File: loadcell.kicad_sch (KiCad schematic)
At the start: 11 parts

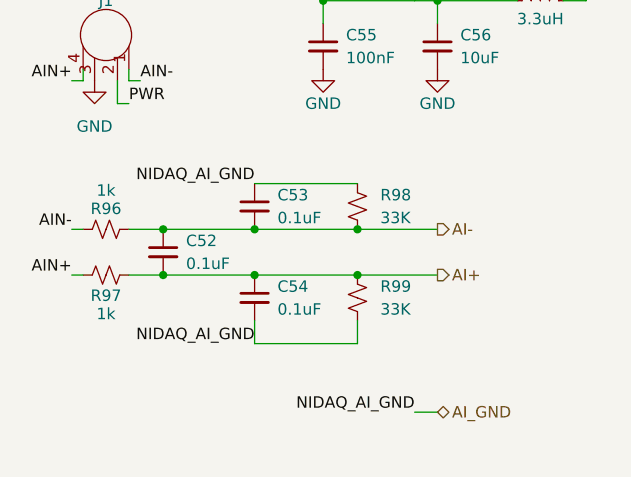
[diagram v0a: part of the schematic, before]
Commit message: Updated schematic. No filtering but besides that finished. Need to fix footprints and start layout.
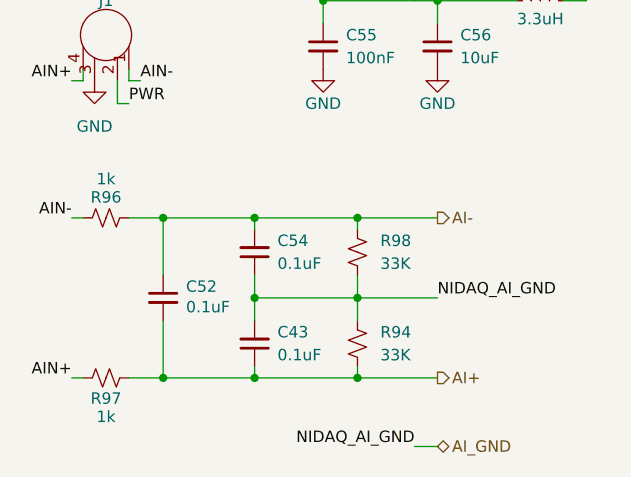
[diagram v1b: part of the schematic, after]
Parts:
- removed C53: 0.1uF, Capacitor_SMD:C_0603_1608Metric, symbol Device:C_Small
- removed R99: 33K, Resistor_SMD:R_0402_1005Metric, symbol Device:R_Small_US
- added C43: 0.1uF, Capacitor_SMD:C_0603_1608Metric, symbol Device:C_Small
- added R94: 33K, Resistor_SMD:R_0402_1005Metric, symbol Device:R_Small_US
- GX-1: footprint UCIRP-KiCAD-Lib:GX16-4 -> 0UCIRP-KiCAD-Lib:GX16-4
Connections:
- net AI+: now also C43.1, R94.1; no longer C54.1
- net AI-: now also C54.2, R98.2; no longer R98.1
- net AI_GND: now also C54.1, R98.1, C43.2, R94.2; no longer C54.2, R98.2
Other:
- moved on the sheet: C52, R96, R97

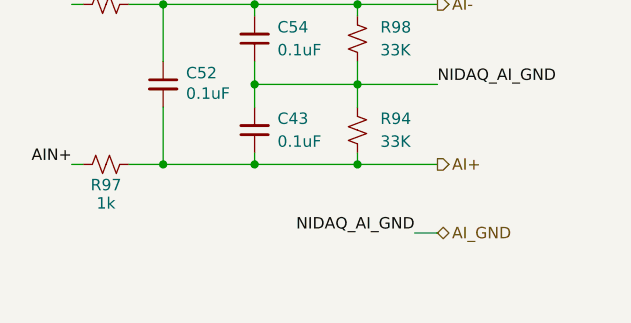
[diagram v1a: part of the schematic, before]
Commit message: Removed extra filtering circuit
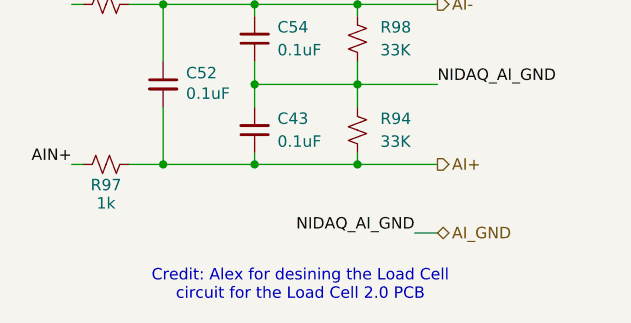
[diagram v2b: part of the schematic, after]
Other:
- note added: "Credit: Alex for desining the Load Cell circuit for the Load Cell 2.0 PCB"
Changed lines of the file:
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@@
 	(generator_version "9.0")
 	(paper "A4")
+	(text "Credit: Alex for desining the Load Cell\ncircuit for the Load Cell 2.0 PCB"
+		(exclude_from_sim no)
+		(at 153.67 135.382 0)
+		(effects
+			(font
+				(size 1.27 1.27)
+			)
+		)
+	)
 	(junction
 		(at 148.59 121.92)

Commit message: Updates after PDR
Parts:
- removed C55: 100nF, Capacitor_SMD:C_0603_1608Metric, symbol Device:C_Small
- removed C56: 10uF, Capacitor_SMD:C_0603_1608Metric, symbol Device:C_Small
- removed L3: 3.3uH, Inductor_SMD:L_0603_1608Metric, symbol Device:L_Small
- C43, C54: value 0.1uF -> 10nF
- C52: value 0.1uF -> 100nF
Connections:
- net PWR renamed +10V_LOAD_CELL

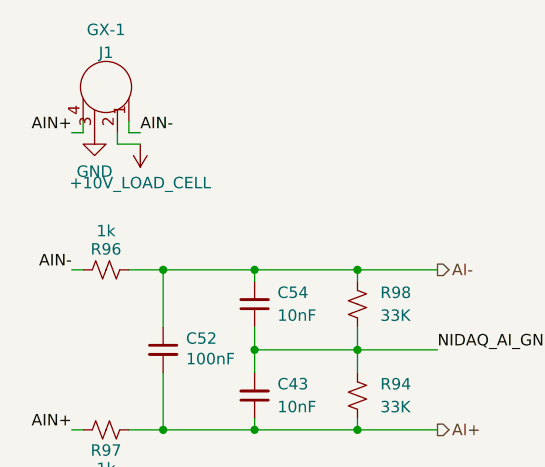
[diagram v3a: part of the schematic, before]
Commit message: Updated to add new filtering circuit
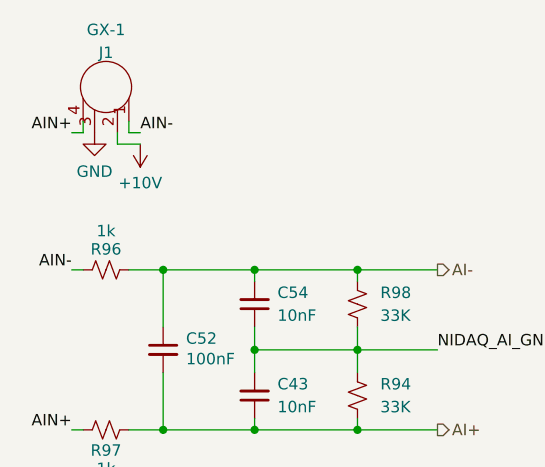
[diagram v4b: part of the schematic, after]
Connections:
- net +10V_LOAD_CELL renamed +10V

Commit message: Subsystem level layout done (prelim)
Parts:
- R94, R98: footprint Resistor_SMD:R_0402_1005Metric -> Resistor_SMD:R_0603_1608Metric
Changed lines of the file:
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@@
 			)
 		)
-		(property "Footprint" "Resistor_SMD:R_0402_1005Metric"
+		(property "Footprint" "Resistor_SMD:R_0603_1608Metric"
 			(at 160.02 107.95 0)
 			(effects
@@
 			)
 		)
-		(property "Footprint" "Resistor_SMD:R_0402_1005Metric"
+		(property "Footprint" "Resistor_SMD:R_0603_1608Metric"
 			(at 160.02 118.11 0)
 			(effects

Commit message: Good progress on full system layout.
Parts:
- C52: value 100nF -> 33nF
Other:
- note added: "Credit: Alex for desining the Load Cell circuit for the Load Cell 2.0 PCB Father Woo for helping me with the filtering calculations"
- note removed: "Credit: Alex for desining the Load Cell circuit for the Load Cell 2.0 PCB"

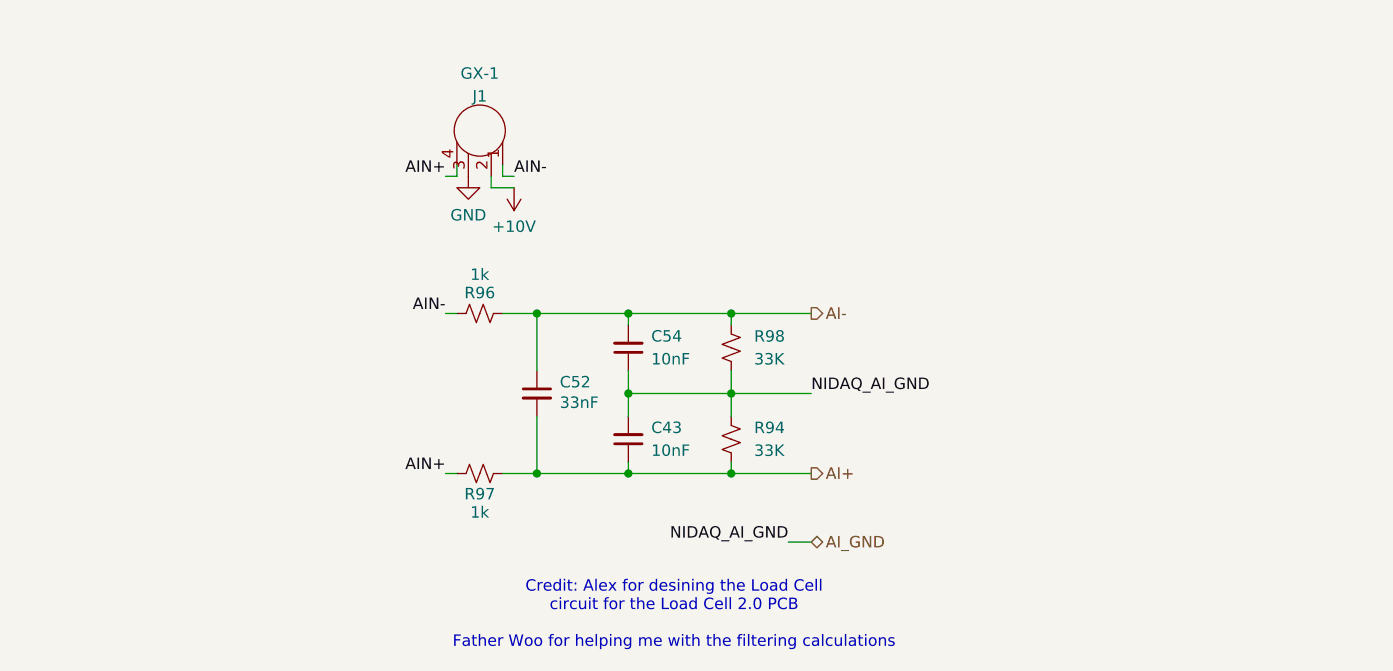
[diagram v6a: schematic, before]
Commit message: GSE v2.1: Updates for DSUB connectors for schematic only done. Layout needs a ton of work
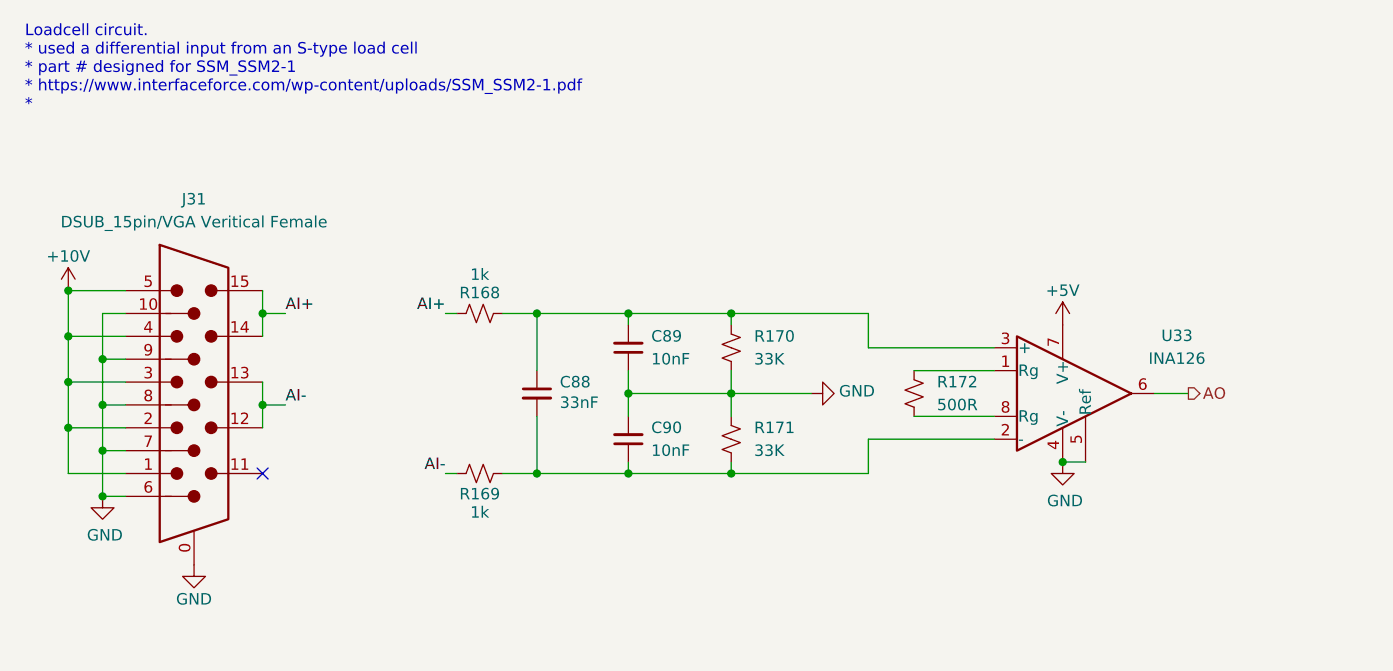
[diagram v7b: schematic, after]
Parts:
- removed C43, C54: 10nF, Capacitor_SMD:C_0603_1608Metric, symbol Device:C_Small
- removed C52: 33nF, Capacitor_SMD:C_0603_1608Metric, symbol Device:C_Small
- removed GX-1: J1, 0UCIRP-KiCAD-Lib:GX16-4, symbol UCIRP-LIB:gx12
- added C88: 33nF, Capacitor_SMD:C_0603_1608Metric, symbol Device:C_Small
- added C89, C90: 10nF, Capacitor_SMD:C_0603_1608Metric, symbol Device:C_Small
- added J31: DSUB_15pin/VGA Veritical Female, 0UCIRP-KiCAD-Lib:Connector_VGA_Vertical, symbol 0UCIRP-KiCAD-Lib:Connector_VGA_vertical
- added R172: 500R, Resistor_SMD:R_0603_1608Metric, symbol Device:R_Small_US
- added U33: INA126, Package_SO:SOIC-8_3.9x4.9mm_P1.27mm, symbol Amplifier_Instrumentation:INA128
- renumbered R96 to R168, R97 to R169, R98 to R170, R94 to R171
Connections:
- net AIN+ is gone; now on net AI-: R169.1
- net AIN- is gone; now on net AI+: R168.2
- net AI_GND is gone; now on net GND: R170.1, R171.2
- net +10V: now also J31.1, J31.2, J31.3, J31.4, J31.5
- net AI+: now also J31.14, J31.15; no longer R169.2, R171.1
- net AI-: now also J31.12, J31.13; no longer R168.1, R170.2
- net GND: now also C89.1, C90.2, J31.0, J31.10, J31.6, J31.7, J31.8, J31.9, U33.4 (V-), U33.5 (Ref)
- new net: R172.2, U33.1 (Rg)
- new net: C88.2, C90.1, R169.2, R171.1, U33.2 (-)
- new net: C88.1, C89.2, R168.1, R170.2, U33.3 (+)
- new net: R172.1, U33.8 (Rg)
- new net +5V: U33.7 (V+)
- new net AO: U33.6
- no-connect marks 0 -> 1
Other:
- note added: "Loadcell circuit. * used a differential input from an S-type load cell * part # designed for SSM_SSM2-1 * https://www.interfaceforce.com/wp-content/uploads/SSM_SSM2-1.pdf *"
- note removed: "Credit: Alex for desining the Load Cell circuit for the Load Cell 2.0 PCB Father Woo for helping me with the filtering calculations"

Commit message: GSE v2.1: placement 70% done, still need to do a lot of routing
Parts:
- added C130: 100nF, Capacitor_SMD:C_0603_1608Metric, symbol Device:C_Small
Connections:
- net +5V: now also C130.1
- net AI+: now also J31.12, J31.13; no longer J31.14, J31.15
- net AI-: now also J31.14, J31.15; no longer J31.12, J31.13
- net GND: now also C130.2
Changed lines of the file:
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@@
 	)
 	(label "AI+"
+		(at 110.49 114.3 0)
+		(effects
+			(font
+				(size 1.27 1.27)
+			)
+			(justify left bottom)
+		)
+	)
+	(label "AI-"
 		(at 110.49 104.14 0)
 		(effects
@@
 			)
 			(justify right bottom)
-		)
-	)
-	(label "AI-"
-		(at 110.49 114.3 0)
-		(effects
-			(font
-				(size 1.27 1.27)
-			)
-			(justify left bottom)
 		)
 	)
@@
 	(symbol
 		(lib_id "Device:C_Small")
+		(at 222.25 113.03 0)
+		(unit 1)
+		(exclude_from_sim no)
+		(in_bom yes)
+		(on_board yes)
+		(dnp no)
+		(property "Reference" "C130"
+			(at 224.79 111.76 0)
+			(effects
+				(font
+					(size 1.27 1.27)
+				)
+				(justify left)
+			)
+		)
+		(property "Value" "100nF"
+			(at 224.79 114.3 0)
+			(effects
+				(font
+					(size 1.27 1.27)
+				)
+				(justify left)
+			)
+		)
+		(property "Footprint" "Capacitor_SMD:C_0603_1608Metric"
+			(at 222.25 113.03 0)
+			(effects
+				(font
+					(size 1.27 1.27)
+				)
+				(hide yes)
+			)
+		)
+		(property "Datasheet" "~"
+			(at 222.25 113.03 0)
+			(effects
+				(font
+					(size 1.27 1.27)
+				)
+				(hide yes)
+			)
+		)
+		(property "Description" ""
+			(at 222.25 113.03 0)
+			(effects
+				(font
+					(size 1.27 1.27)
+				)
+			)
+		)
+		(property "Manufacturer" "Generic"
+			(at 222.25 113.03 0)
+			(effects
+				(font
+					(size 1.27 1.27)
+				)
+				(hide yes)
+			)
+		)
+		(property "Part #" "Generic 100nF 6.3V X7R 0402 MLCC"
+			(at 222.25 113.03 0)
+			(effects
+				(font
+					(size 1.27 1.27)
+				)
+				(hide yes)
+			)
+		)
+		(pin "1"
+		)
+		(pin "2"
+		)
+		(instances
+			(project "gse2-hardware"
+				(path "/1eb2a3ff-e0fd-4343-8dba-716780a4d459/2fe13bef-73c1-4e16-ae42-c92f73f4444c"
+					(reference "C131")
+					(unit 1)
+				)
+				(path "/1eb2a3ff-e0fd-4343-8dba-716780a4d459/bbd1f9c2-41a9-4d87-bcf9-61e538da6258"
+					(reference "C130")
+					(unit 1)
+				)
+			)
+		)
+	)
+	(symbol
+		(lib_id "Device:C_Small")
 		(at 138.43 113.03 0)
 		(unit 1)
@@
 	)
 	(symbol
+		(lib_id "power:GND")
+		(at 222.25 115.57 0)
+		(unit 1)
+		(exclude_from_sim no)
+		(in_bom yes)
+		(on_board yes)
+		(dnp no)
+		(property "Reference" "#PWR091"
+			(at 222.25 121.92 0)
+			(effects
+				(font
+					(size 1.27 1.27)
+				)
+				(hide yes)
+			)
+		)
+		(property "Value" "GND"
+			(at 222.25 119.38 0)
+			(effects
+				(font
+					(size 1.27 1.27)
+				)
+			)
+		)
+		(property "Footprint" ""
+			(at 222.25 115.57 0)
+			(effects
+				(font
+					(size 1.27 1.27)
+				)
+				(hide yes)
+			)
+		)
+		(property "Datasheet" ""
+			(at 222.25 115.57 0)
+			(effects
+				(font
+					(size 1.27 1.27)
+				)
+				(hide yes)
+			)
+		)
+		(property "Description" ""
+			(at 222.25 115.57 0)
+			(effects
+				(font
+					(size 1.27 1.27)
+				)
+			)
+		)
+		(pin "1"
+		)
+		(instances
+			(project "gse2-hardware"
+				(path "/1eb2a3ff-e0fd-4343-8dba-716780a4d459/2fe13bef-73c1-4e16-ae42-c92f73f4444c"
+					(reference "#PWR0113")
+					(unit 1)
+				)
+				(path "/1eb2a3ff-e0fd-4343-8dba-716780a4d459/bbd1f9c2-41a9-4d87-bcf9-61e538da6258"
+					(reference "#PWR091")
+					(unit 1)
+				)
+			)
+		)
+	)
+	(symbol
 		(lib_id "Device:R_Small_US")
 		(at 132.08 121.92 90)
@@
 					(unit 1)
 				)
+			)
+		)
+	)
+	(symbol
+		(lib_name "+3.3V_11")
+		(lib_id "power:+3.3V")
+		(at 222.25 110.49 0)
+		(unit 1)
+		(exclude_from_sim no)
+		(in_bom yes)
+		(on_board yes)
+		(dnp no)
+		(property "Reference" "#PWR080"
+			(at 222.25 114.3 0)
+			(effects
+				(font
+					(size 1.27 1.27)
+				)
+				(hide yes)
+			)
+		)
+		(property "Value" "+5V"
+			(at 222.25 106.68 0)
+			(effects
+				(font
+					(size 1.27 1.27)
+				)
+			)
+		)
+		(property "Footprint" ""
+			(at 222.25 110.49 0)
+			(effects
+				(font
+					(size 1.27 1.27)
+				)
+				(hide yes)
+			)
+		)
+		(property "Datasheet" ""
+			(at 222.25 110.49 0)
+			(effects
+				(font
+					(size 1.27 1.27)
+				)
+				(hide yes)
+			)
+		)
+		(property "Description" ""
+			(at 222.25 110.49 0)
+			(effects
+				(font
+					(size 1.27 1.27)
+				)
+			)
+		)
+		(pin "1"
+		)
+		(instances
+			(project "gse2-hardware"
+				(path "/1eb2a3ff-e0fd-4343-8dba-716780a4d459/2fe13bef-73c1-4e16-ae42-c92f73f4444c"
+					(reference "#PWR0102")
+					(unit 1)
+				)
+				(path "/1eb2a3ff-e0fd-4343-8dba-716780a4d459/bbd1f9c2-41a9-4d87-bcf9-61e538da6258"
+					(reference "#PWR080")
+					(unit 1)
+				)
